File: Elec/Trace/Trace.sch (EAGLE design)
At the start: 39 parts, among them IC1 L298, IC2 L298, U1 SN74HC595N, U2 SN74HC595N

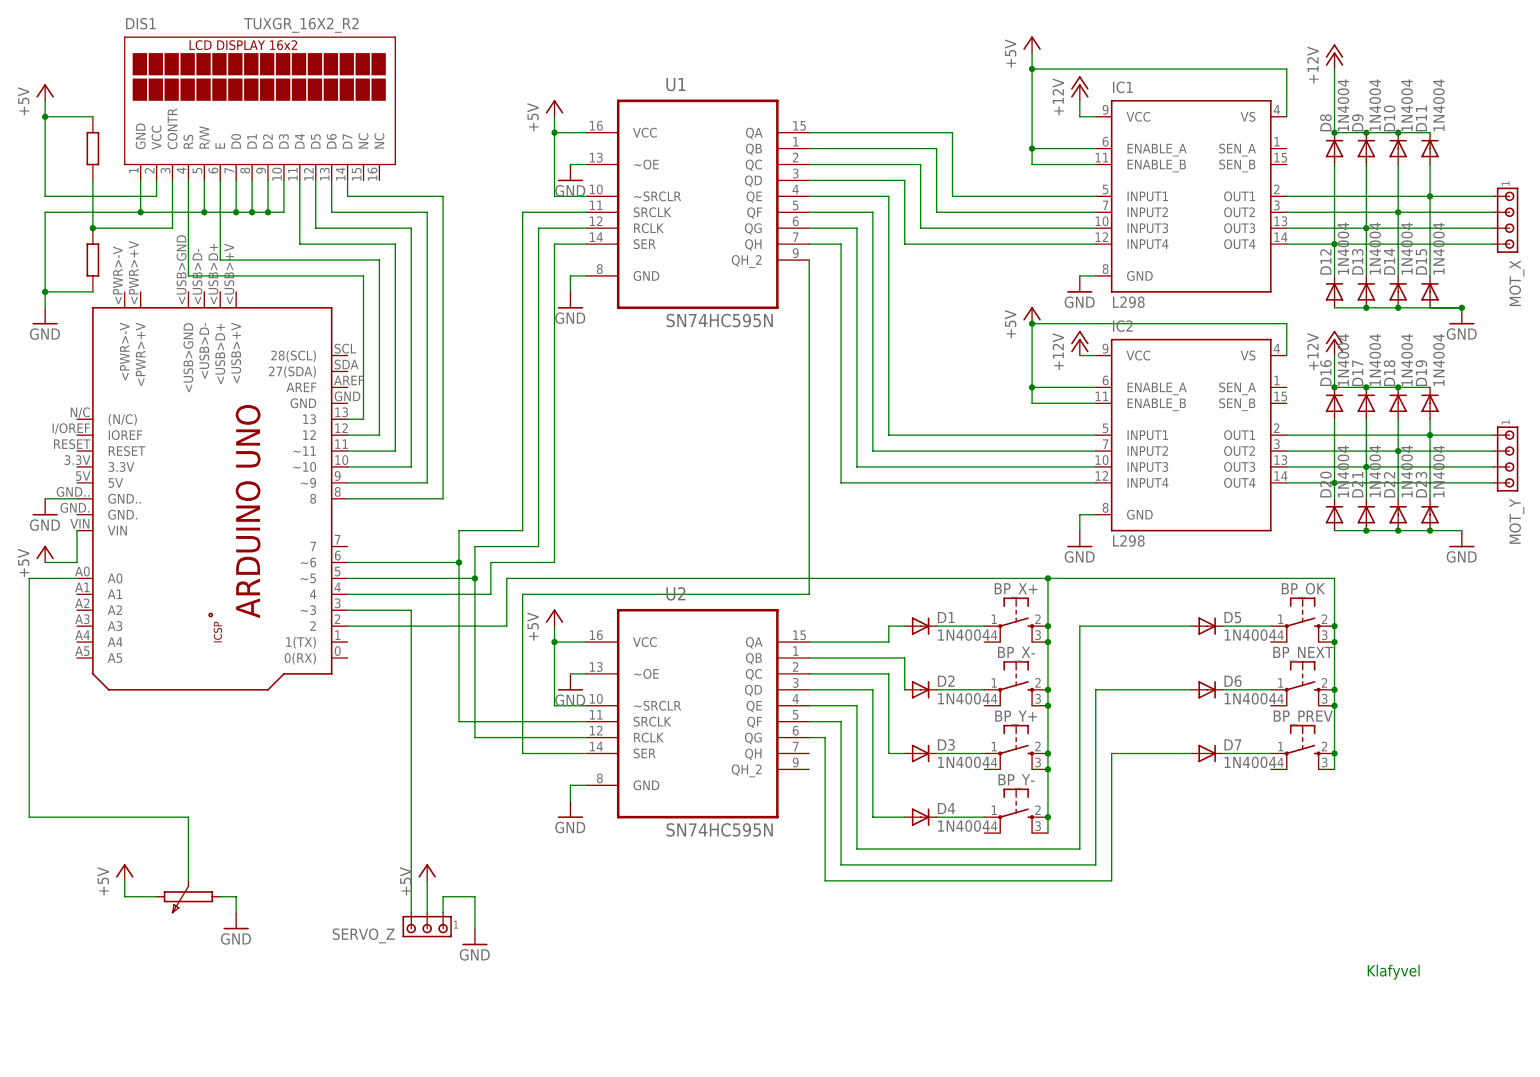
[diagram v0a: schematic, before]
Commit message: Ajout du nom du site dans le schéma.
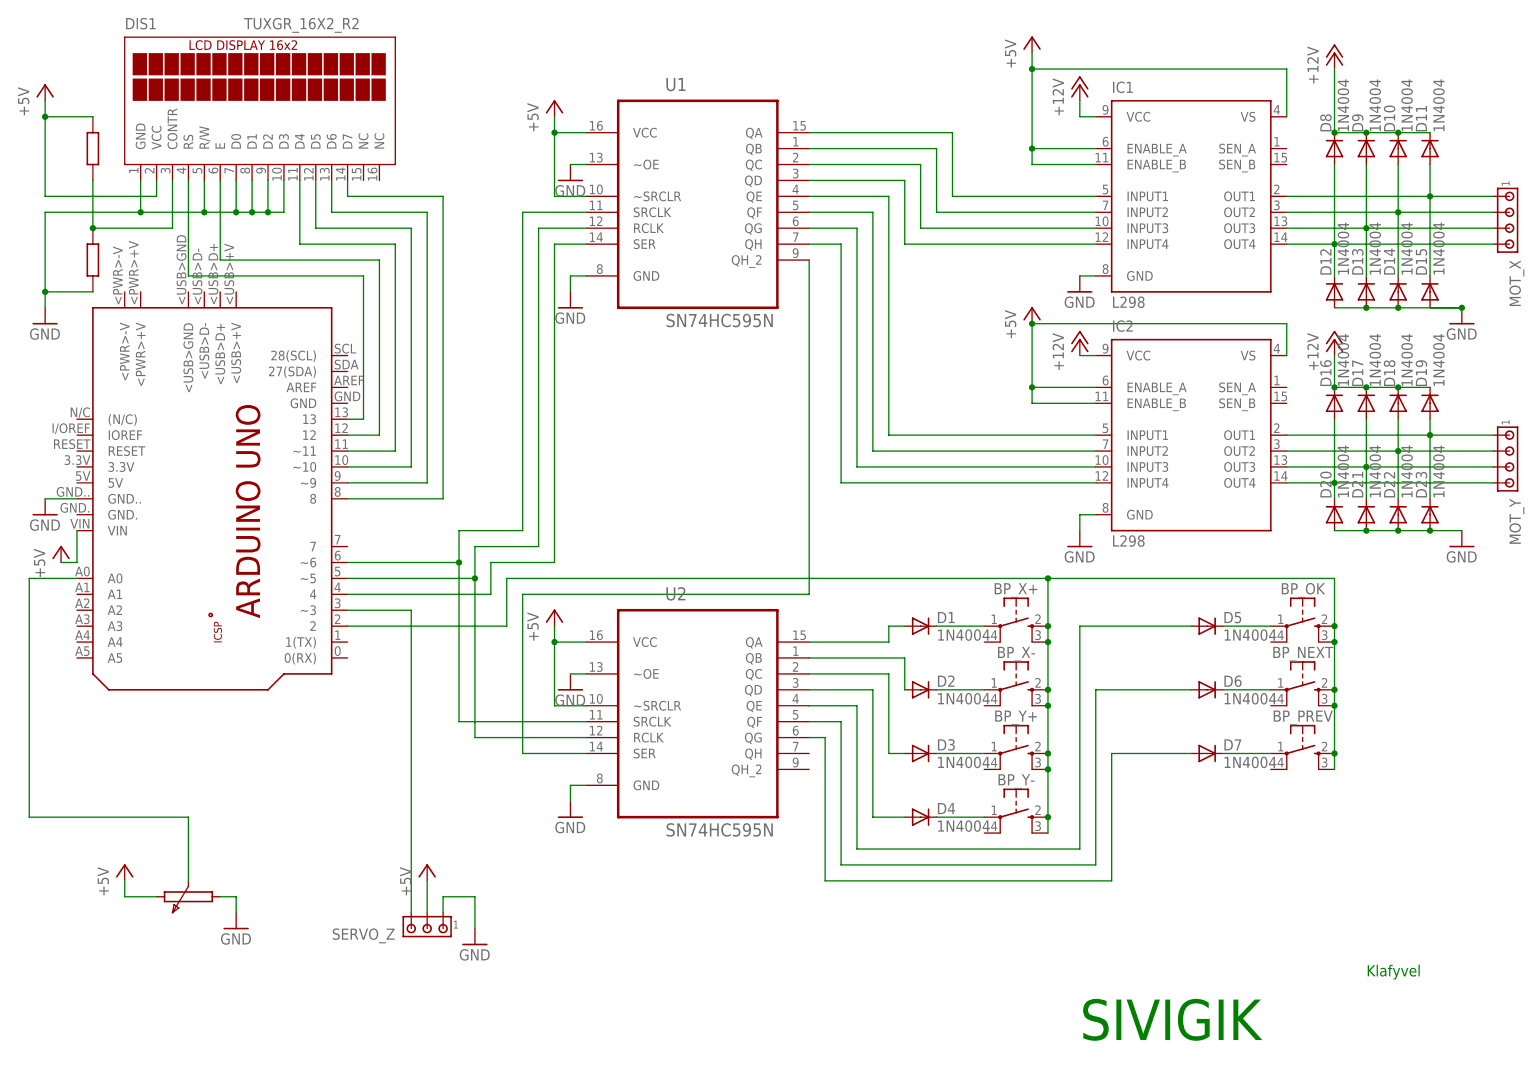
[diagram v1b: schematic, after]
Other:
- note added: "SIVIGIK"
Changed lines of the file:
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@@
 <plain>
 <text x="218.44" y="20.32" size="1.778" layer="91">Klafyvel</text>
+<text x="172.72" y="10.16" size="6.4516" layer="91" ratio="29">SIVIGIK</text>
 </plain>
 <instances>
@@
 <instance part="P+2" gate="1" x="172.72" y="162.56"/>
 <instance part="P+3" gate="1" x="88.9" y="160.02"/>
-<instance part="P+4" gate="1" x="7.62" y="88.9"/>
+<instance part="P+4" gate="1" x="10.16" y="88.9"/>
 <instance part="P+5" gate="1" x="68.58" y="38.1"/>
 <instance part="GND1" gate="1" x="76.2" y="25.4"/>
@@
 <pinref part="P+4" gate="1" pin="+5V"/>
 <pinref part="PCB1" gate="G$1" pin="VIN"/>
-<wire x1="7.62" y1="86.36" x2="12.7" y2="86.36" width="0.1524" layer="91"/>
+<wire x1="10.16" y1="86.36" x2="12.7" y2="86.36" width="0.1524" layer="91"/>
 <wire x1="12.7" y1="86.36" x2="12.7" y2="91.44" width="0.1524" layer="91"/>
 </segment>
